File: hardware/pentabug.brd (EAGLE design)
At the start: 82.9 x 33 mm, 19 parts, among them IC1 ATMEGA88

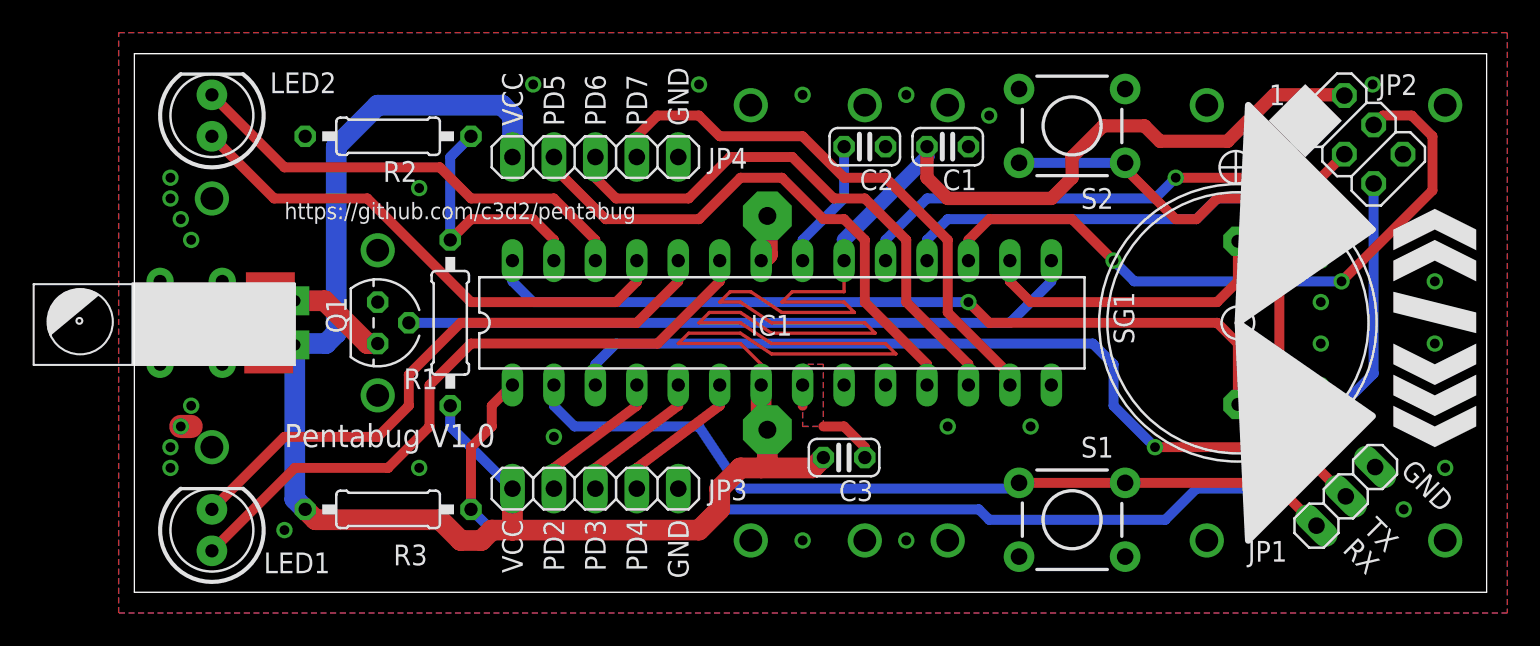
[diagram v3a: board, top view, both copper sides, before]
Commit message: better connection for AVcc block capacitor, Moar vias FTW!
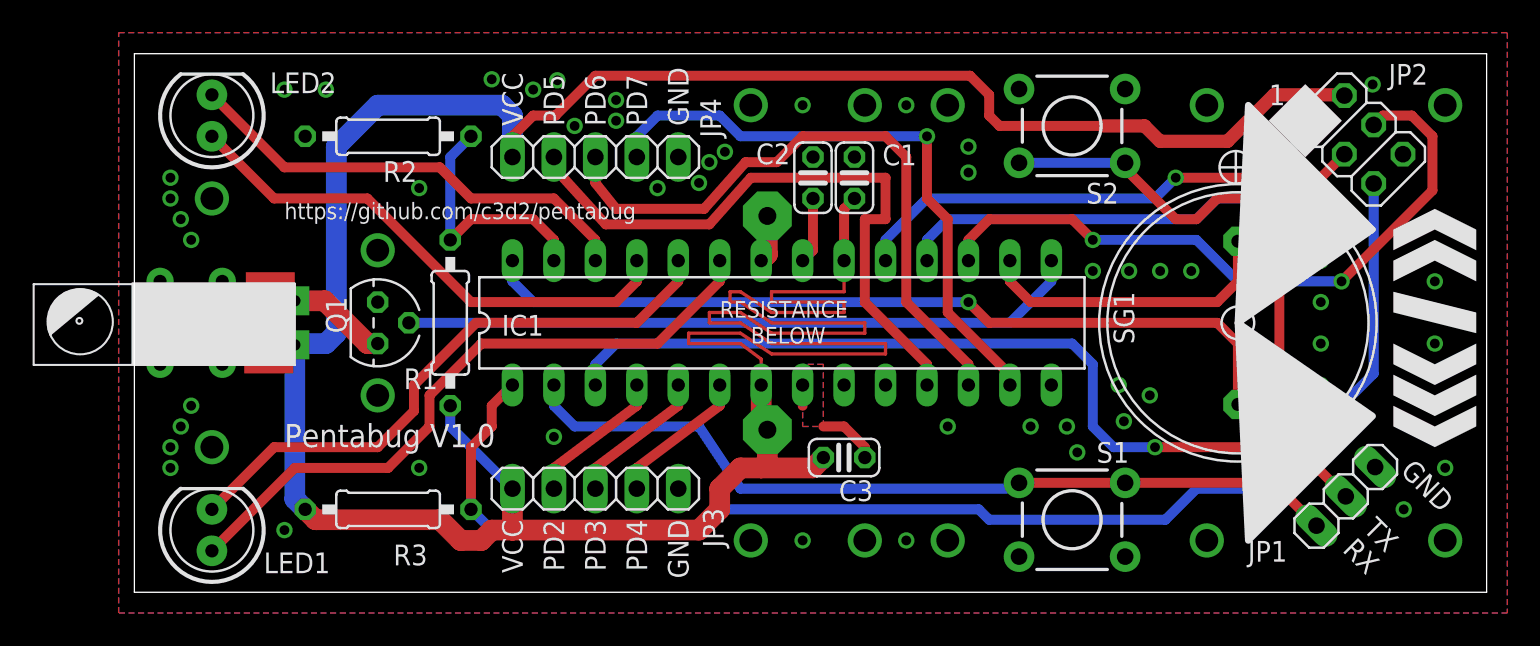
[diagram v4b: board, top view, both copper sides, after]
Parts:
- moved C1 6.02 mm to (45.1, 25.4), turned to 270 degrees
- moved C2 3.70 mm to (42.5, 25.4), turned to 270 degrees
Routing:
- net VCC: track 205.3 -> 221.8 mm
- net PD5: track 34.1 -> 39.3 mm
- net PD6: track 34.5 -> 39.4 mm
- net N$17: track 8.04 -> 4.07 mm
- net PD7: track 34.5 -> 37.4 mm, vias 0 -> 1
- net TX: track 86.0 -> 86.7 mm
- net GND: track 8.50 -> 7.87 mm, vias 44 -> 64
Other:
- board text added: "BELOW"
- board text added: "RESISTANCE"

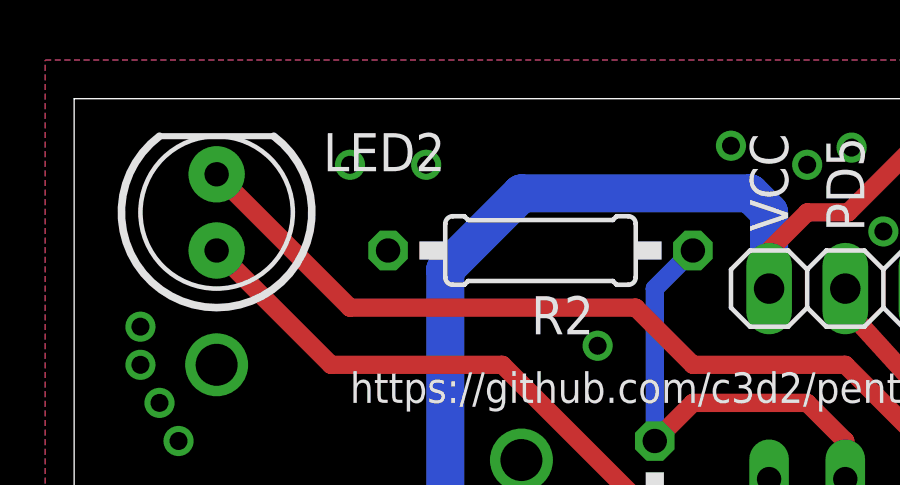
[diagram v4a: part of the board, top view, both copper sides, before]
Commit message: moved vias away from print for LED2
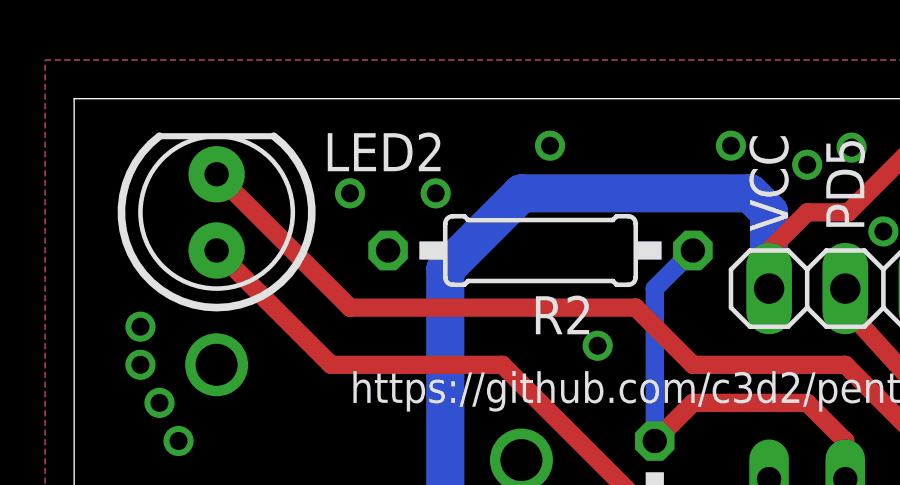
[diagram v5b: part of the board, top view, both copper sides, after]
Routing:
- net GND: vias 64 -> 65
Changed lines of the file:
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@@
 <via x="27.94" y="28.575" extent="1-16" drill="0.6"/>
 <via x="30.48" y="30.1625" extent="1-16" drill="0.6"/>
-<via x="10.16" y="30.7975" extent="1-16" drill="0.6"/>
-<via x="12.7" y="30.7975" extent="1-16" drill="0.6"/>
+<via x="10.16" y="29.845" extent="1-16" drill="0.6"/>
+<via x="13.0175" y="29.845" extent="1-16" drill="0.6"/>
 <via x="52.07" y="27.305" extent="1-16" drill="0.6"/>
 <via x="52.07" y="25.7175" extent="1-16" drill="0.6"/>
@@
 <via x="61.2775" y="12.7" extent="1-16" drill="0.6"/>
 <via x="63.1825" y="12.065" extent="1-16" drill="0.6"/>
+<via x="16.8275" y="31.4325" extent="1-16" drill="0.6"/>
 </signal>
 <signal name="N$17">

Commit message: some schematics beautification
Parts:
- R2: value 18K -> 22K
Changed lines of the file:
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@@
 <element name="SG1" library="buglbr" package="BUZZRTDK" value="MULTIBUZZRTDKBUZZR" x="68.58" y="16.51" smashed="yes" rot="R90">
 <attribute name="NAME" x="60.96" y="18.415" size="1.27" layer="25" font="vector" ratio="10" rot="R270"/>
-<attribute name="VALUE" x="76.2" y="11.43" size="1.778" layer="27" ratio="10" rot="R90"/>
 </element>
 <element name="R1" library="rcl" package="0207/10" value="100K" x="20.32" y="16.51" smashed="yes" rot="R90">
@@
 <attribute name="VALUE" x="20.955" y="14.2494" size="1.27" layer="27" ratio="10" rot="R90"/>
 </element>
-<element name="R2" library="rcl" package="0207/10" value="18K" x="16.51" y="27.94" smashed="yes" rot="R180">
+<element name="R2" library="rcl" package="0207/10" value="22K" x="16.51" y="27.94" smashed="yes" rot="R180">
 <attribute name="NAME" x="18.288" y="26.416" size="1.27" layer="25" font="vector" ratio="10" rot="R180"/>
 <attribute name="VALUE" x="18.7706" y="28.575" size="1.27" layer="27" ratio="10" rot="R180"/>
@@
 </signal>
 </signals>
-<errors>
-</errors>
 </board>
 </drawing>
